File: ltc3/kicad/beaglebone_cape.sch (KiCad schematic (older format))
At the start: 17 parts, among them U301 24C256, U302 LTC2991, U303 LTC2991

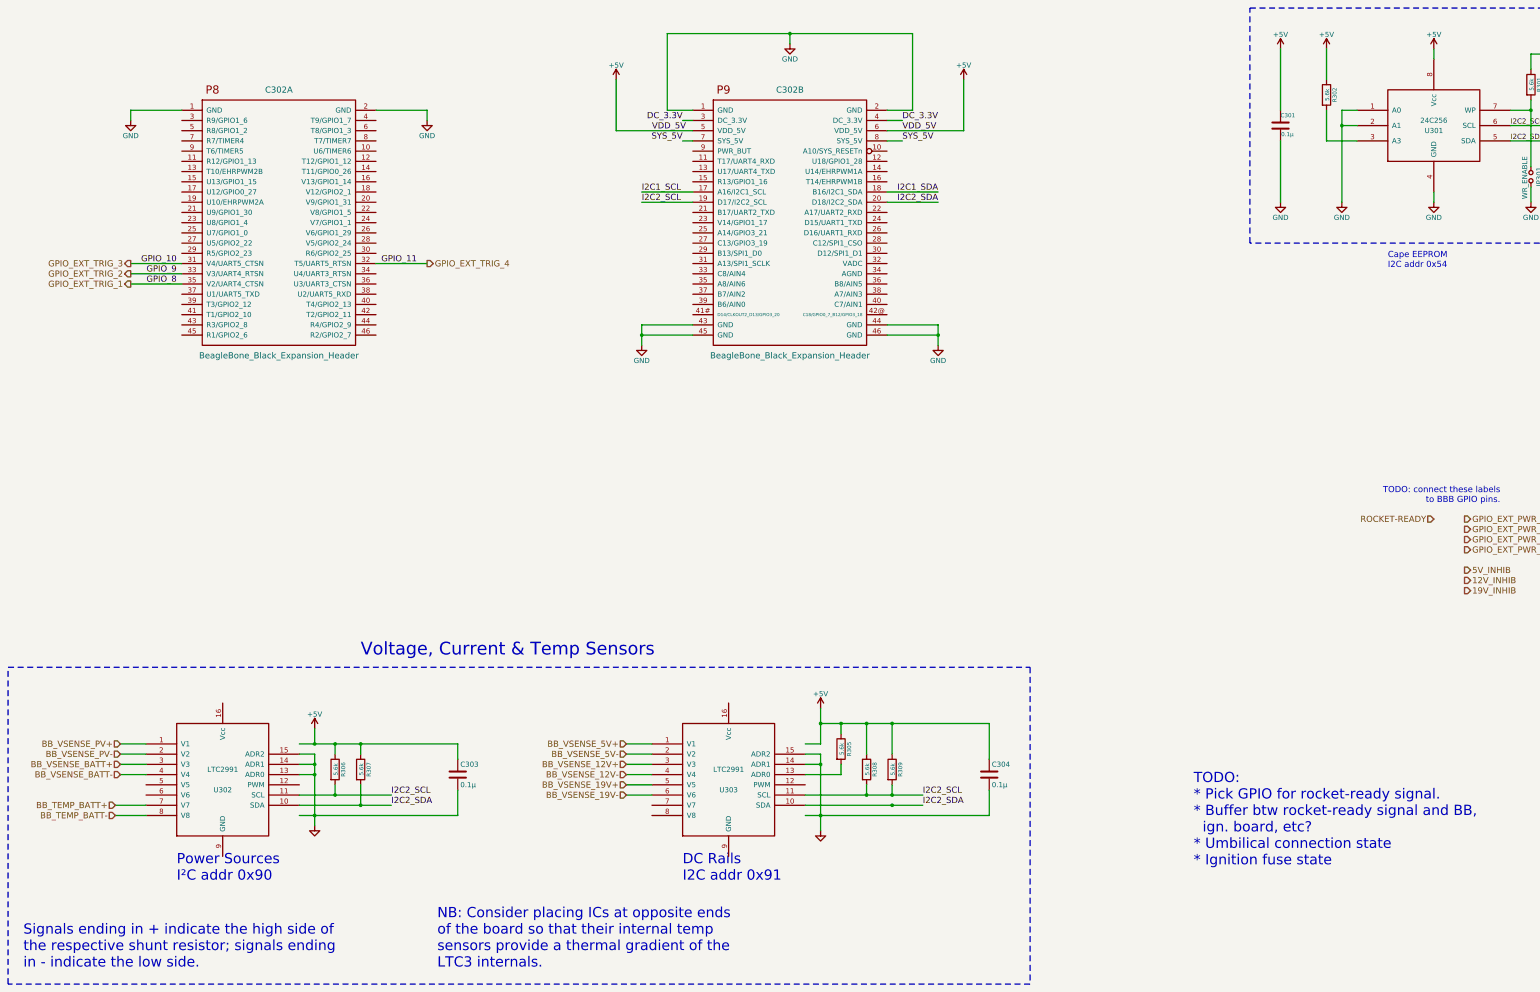
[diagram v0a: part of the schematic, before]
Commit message: LTC3: Cleaned up external devices schematic; other minor cosmetic edits.
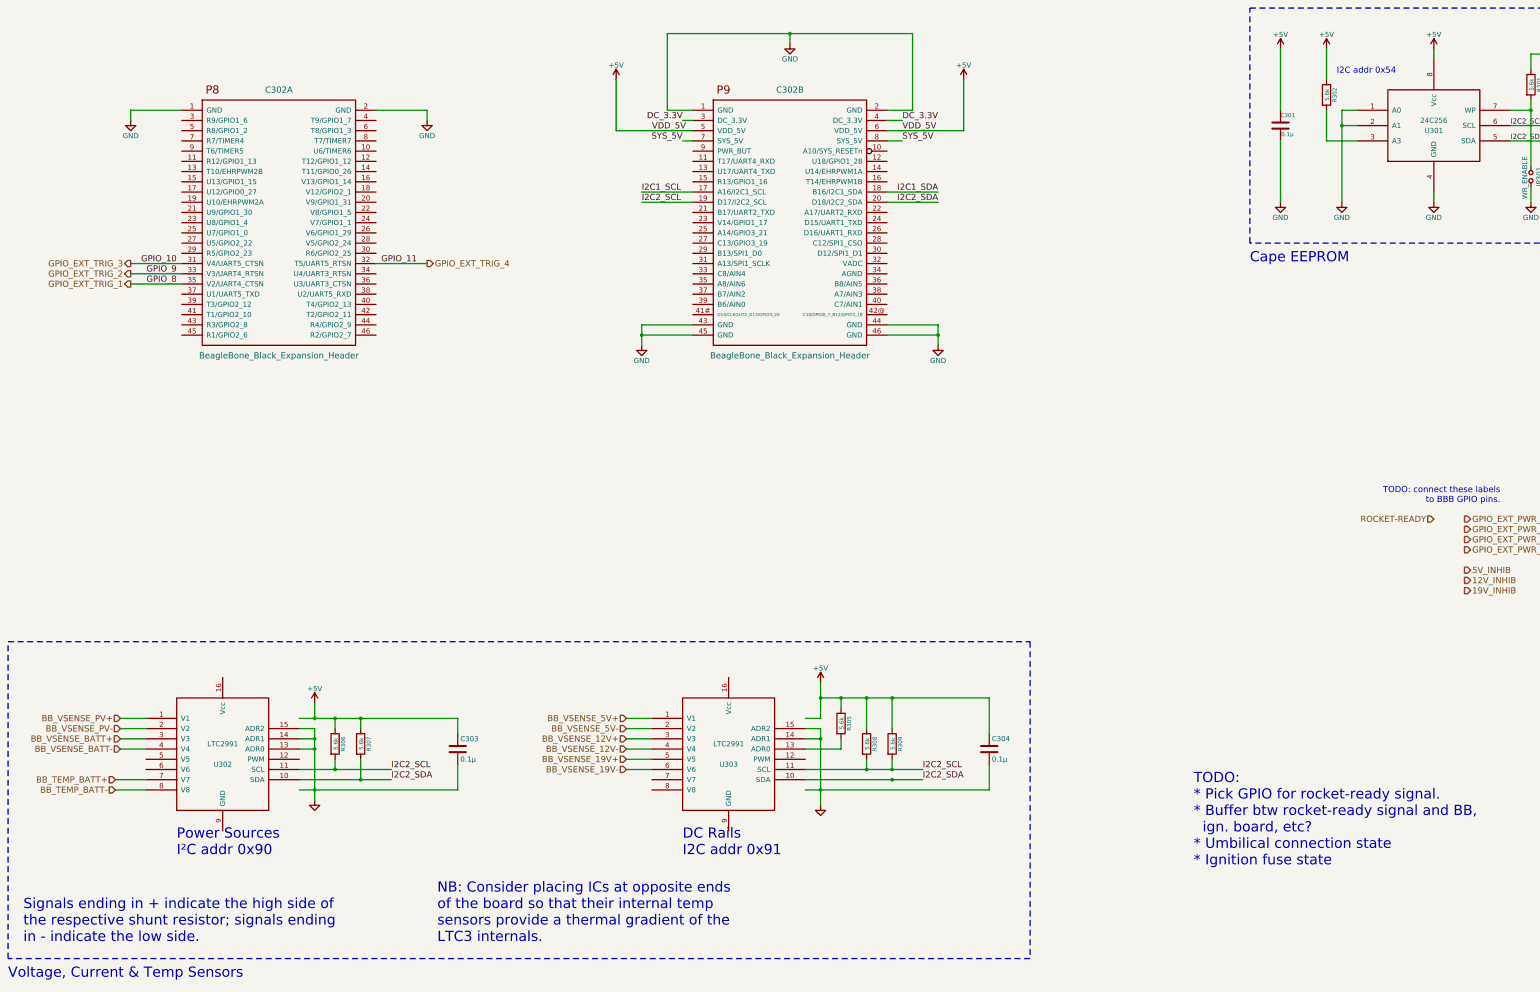
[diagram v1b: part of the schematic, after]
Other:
- note added: "Cape EEPROM"
- note added: "I2C addr 0x54"
- note removed: "Cape EEPROM\nI2C addr 0x54"
- moved on the sheet: C303, C304, R305, R306, R307, R308, R309, U302, U303

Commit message: LTC3: Renamed external device related hierarchical pins.
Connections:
- net labels added: EXT_PWR_EN_1, EXT_PWR_EN_2, EXT_PWR_EN_3, EXT_PWR_EN_4, EXT_TRIG_EN_1, EXT_TRIG_EN_2, EXT_TRIG_EN_3, EXT_TRIG_EN_4, ROCKET_READY
- net labels removed: GPIO_EXT_PWR_1, GPIO_EXT_PWR_2, GPIO_EXT_PWR_3, GPIO_EXT_PWR_4, GPIO_EXT_TRIG_1, GPIO_EXT_TRIG_2, GPIO_EXT_TRIG_3, GPIO_EXT_TRIG_4, ROCKET-READY
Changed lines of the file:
@@
 GPIO_9
 Text HLabel 1900 3450 0    60   Output ~ 0
-GPIO_EXT_TRIG_1
+EXT_TRIG_EN_1
 Text HLabel 1900 3350 0    60   Output ~ 0
-GPIO_EXT_TRIG_2
+EXT_TRIG_EN_2
 Text HLabel 1900 3250 0    60   Output ~ 0
-GPIO_EXT_TRIG_3
+EXT_TRIG_EN_3
 Text HLabel 4800 3250 2    60   Output ~ 0
-GPIO_EXT_TRIG_4
+EXT_TRIG_EN_4
 Text HLabel 14950 5750 2    60   Output ~ 0
-GPIO_EXT_PWR_1
+EXT_PWR_EN_1
 Text HLabel 14950 5850 2    60   Output ~ 0
-GPIO_EXT_PWR_2
+EXT_PWR_EN_2
 Text HLabel 14950 5950 2    60   Output ~ 0
-GPIO_EXT_PWR_3
+EXT_PWR_EN_3
 Text HLabel 14950 6050 2    60   Output ~ 0
-GPIO_EXT_PWR_4
+EXT_PWR_EN_4
 Text Notes 15300 5600 2    60   ~ 0
 TODO: connect these labels\nto BBB GPIO pins.
@@
 NB: Consider placing ICs at opposite ends\nof the board so that their internal temp\nsensors provide a thermal gradient of the\nLTC3 internals.
 Text HLabel 14650 5750 0    60   Input ~ 0
-ROCKET-READY
+ROCKET_READY
 $Comp
 L +5V #PWR307

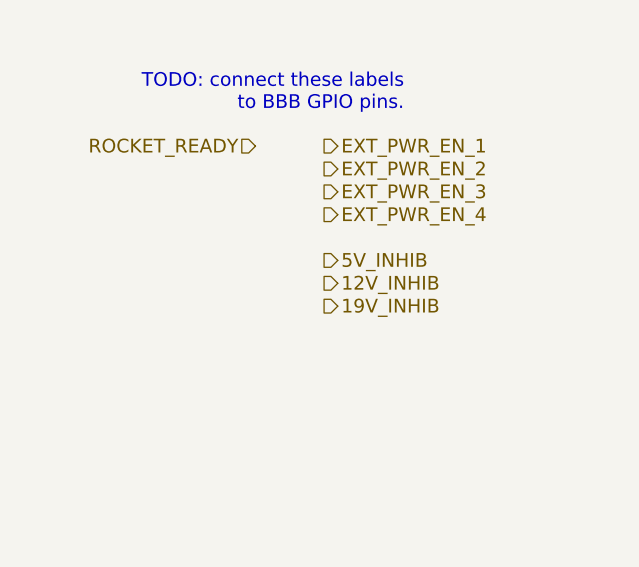
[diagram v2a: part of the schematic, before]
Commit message: LTC3: Renamed DC/DC converter-enabling hierachical pins.
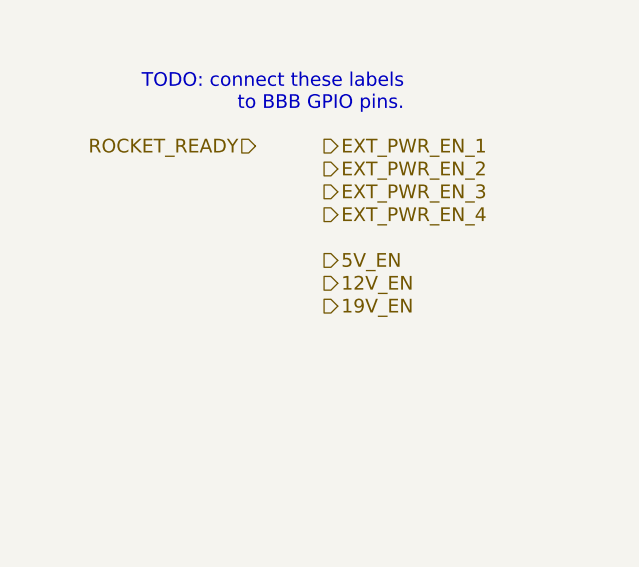
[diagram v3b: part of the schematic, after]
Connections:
- net labels added: 12V_EN, 19V_EN, 5V_EN
- net labels removed: 12V_INHIB, 19V_INHIB, 5V_INHIB
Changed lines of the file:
@@
 $EndComp
 Text HLabel 14950 6250 2    60   Output ~ 0
-5V_INHIB
+5V_EN
 Text HLabel 14950 6350 2    60   Output ~ 0
-12V_INHIB
+12V_EN
 Text HLabel 14950 6450 2    60   Output ~ 0
-19V_INHIB
+19V_EN
 Text HLabel 1750 8300 0    60   Input ~ 0
 BB_TEMP_BATT+

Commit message: LTC3: Moved DC rail sense IC; more hierarchical pin edits.
1. Moved DC rail-sensing LTC2991 IC from the BeagleBone sheet to the
   DC/DC converter sheet.  Makes the top-level sheet easier to read.
2. More adjustments to related hierarchical pins.
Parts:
- removed C304: 0.1μ, symbol C
- removed R303, R304, R305, R308, R309: 5.6k, ~, symbol R
- removed U303: LTC2991, symbol LTC2991
- added R? (x2): 5.6k, ~, symbol R
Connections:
- net labels removed: BB_VSENSE_12V+, BB_VSENSE_12V-, BB_VSENSE_19V+, BB_VSENSE_19V-, BB_VSENSE_5V+, BB_VSENSE_5V-, I2C1_SCL, I2C1_SDA
- wire segments 99 -> 85
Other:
- note removed: "DC Rails\nI2C addr 0x91"
- note removed: "Signals ending in + indicate the high side of\nthe respective shunt resistor; signals ending\nin - indicate the low side."

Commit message: LTC3: Moved input voltage/current sensing from BB schematic to charging schematic.
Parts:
- removed C303: 0.1μ, symbol C
- removed R306, R307: 5.6k, ~, symbol R
- removed U302: LTC2991, symbol LTC2991
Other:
- note added: "BeagleBone Expansion Headers"
- note removed: "NB: Consider placing ICs at opposite ends\nof the board so that their internal temp\nsensors provide a thermal gradient of the\nLTC3 internals."
- note removed: "Power Sources\nI²C addr 0x90"
- note removed: "Voltage, Current & Temp Sensors"
- moved on the sheet: C301, C302A, C302B, JP301, R301, R302, R?, U301
